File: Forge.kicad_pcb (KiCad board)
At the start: 2 copper layers, 2 parts, among them J1 USB_C_Receptacle_USB2.0_14P, U1 STM32F301C6Tx

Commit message: Began basic power design
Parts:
- added R1: 5k1, Resistor_SMD:R_0805_2012Metric_Pad1.20x1.40mm_HandSolder, F.Cu at (115.5, 99.0)
- added R2: 5k1, Resistor_SMD:R_0805_2012Metric_Pad1.20x1.40mm_HandSolder, F.Cu at (115.5, 101.9)
- added U2: AP2112K-3.3, Package_TO_SOT_SMD:SOT-23-5, F.Cu at (110.6, 99.9)
- added U3: USBLC6-2SC6, Package_TO_SOT_SMD:SOT-23-6, F.Cu at (110.6, 104.5)
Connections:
- net Net-(J1-GND-PadA1) renamed GND
- net Net-(J1-VBUS-PadA4) renamed +5V
- J1 pad A5: unconnected-(J1-CC1-PadA5) -> CC1
- J1 pad A6: unconnected-(J1-D+-PadA6) -> USB_Conn_D-
- J1 pad A7: unconnected-(J1-D--PadA7) -> USB_Conn_D+
- J1 pad B5: unconnected-(J1-CC2-PadB5) -> CC2
- J1 pad B6: unconnected-(J1-D+-PadB6) -> USB_Conn_D-
- J1 pad B7: unconnected-(J1-D--PadB7) -> USB_Conn_D+

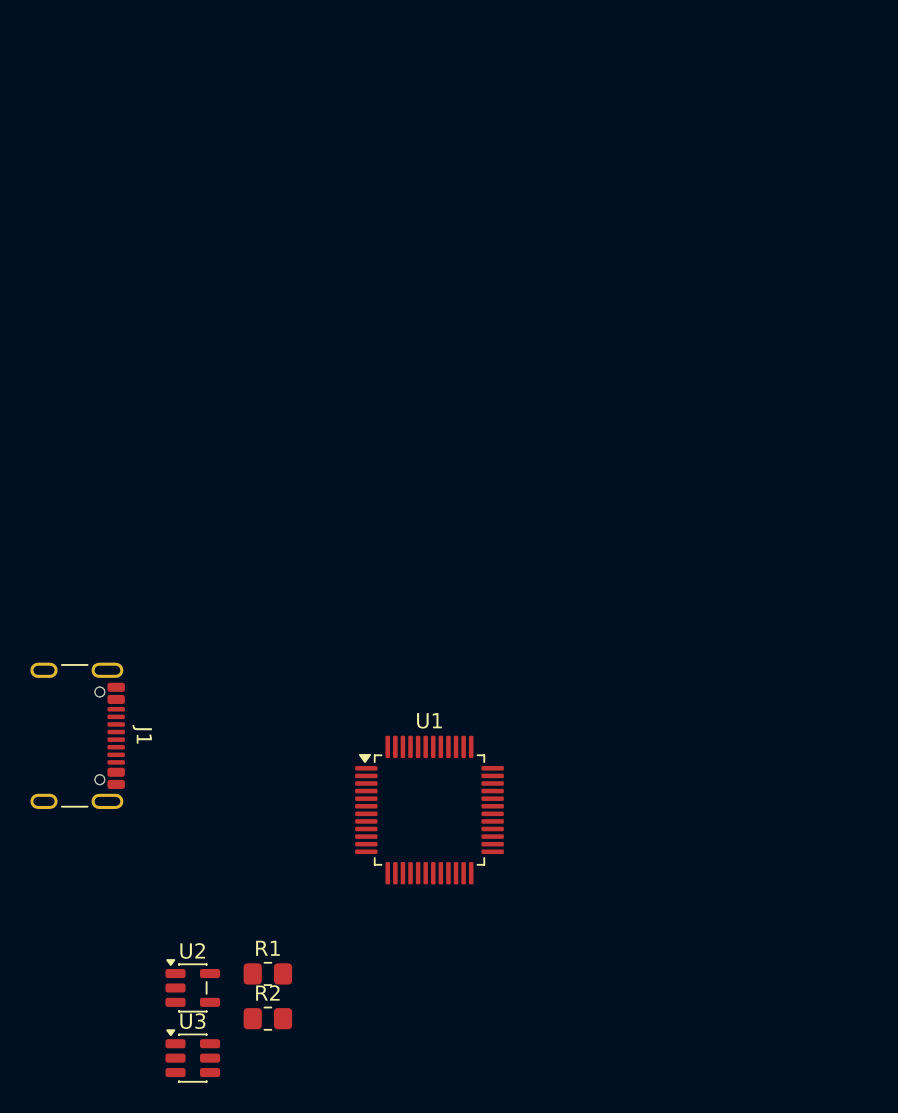
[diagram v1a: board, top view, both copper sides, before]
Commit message: Changed to MCU from stm32 to esp32 wroom for easier use for a first board
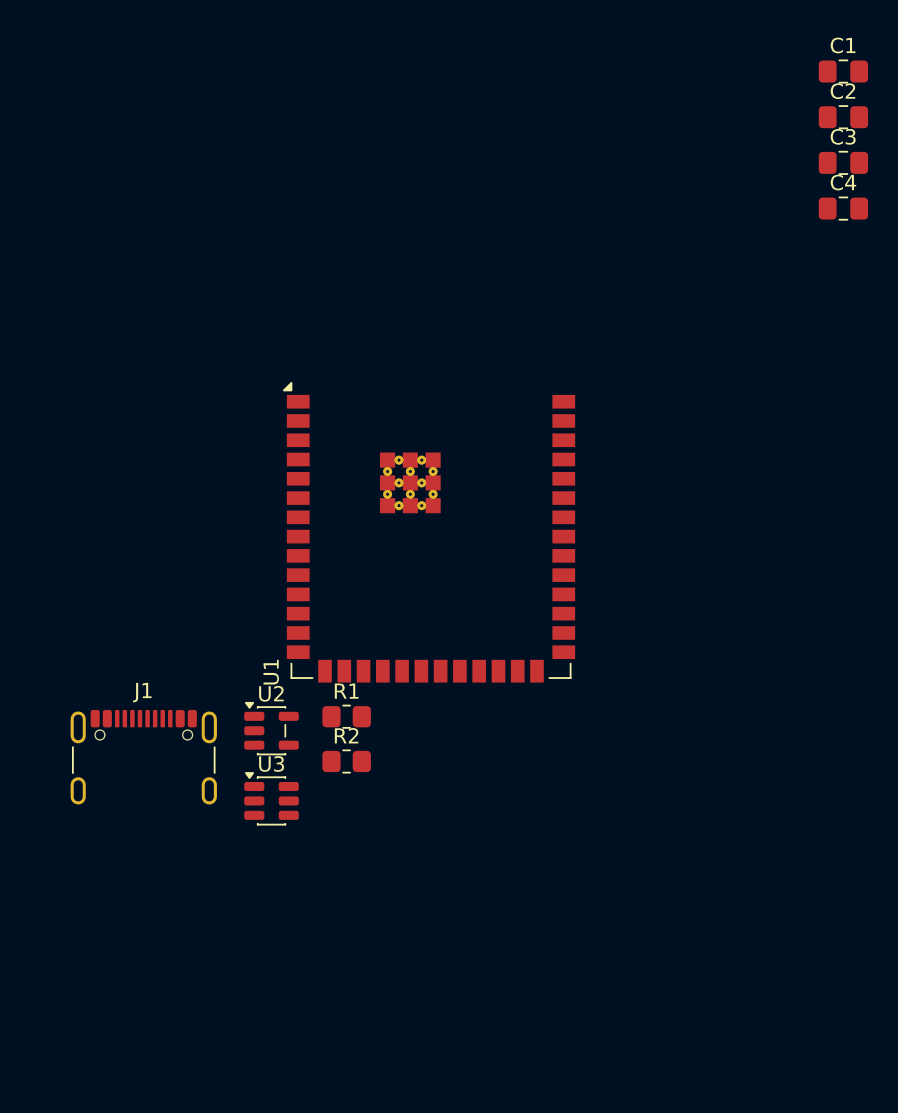
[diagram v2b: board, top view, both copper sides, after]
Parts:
- added C1: 1u, Capacitor_SMD:C_0805_2012Metric_Pad1.18x1.45mm_HandSolder, F.Cu at (153.5, 39.5)
- added C2: 1u, Capacitor_SMD:C_0805_2012Metric_Pad1.18x1.45mm_HandSolder, F.Cu at (153.5, 42.5)
- added C3: 100n, Capacitor_SMD:C_0805_2012Metric_Pad1.18x1.45mm_HandSolder, F.Cu at (153.5, 45.5)
- added C4: 10u, Capacitor_SMD:C_0805_2012Metric_Pad1.18x1.45mm_HandSolder, F.Cu at (153.5, 48.5)
- U1: value STM32F301C6Tx -> ESP32-S3-WROOM-2; footprint Package_QFP:LQFP-48_7x7mm_P0.5mm -> RF_Module:ESP32-S3-WROOM-2
- moved U1 21.7 mm to (126.3, 66.5)
- moved R2 17.7 mm to (120.7, 85.0)
- moved U2 17.7 mm to (115.8, 83.0)
- moved U3 17.7 mm to (115.8, 87.6)
- moved R1 17.7 mm to (120.7, 82.0)
- moved J1 6.06 mm to (107.3, 85.8), turned to 0 degrees
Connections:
- U1 pad 1: unconnected-(U1-VBAT-Pad1) -> GND
- U1 pad 12: unconnected-(U1-PA2-Pad12) -> I2C_SDA
- U1 pad 13: unconnected-(U1-PA3-Pad13) -> USB_D-
- U1 pad 14: unconnected-(U1-PA4-Pad14) -> USB_D+
- U1 pad 17: unconnected-(U1-PA7-Pad17) -> I2C_SCL
- U1 pad 18: unconnected-(U1-PB0-Pad18) -> SPI_CLK
- U1 pad 19: unconnected-(U1-PB1-Pad19) -> SPI_MOSI
- U1 pad 2: unconnected-(U1-PC13-Pad2) -> +3.3V
- U1 pad 20: unconnected-(U1-PB2-Pad20) -> SPI_MISO
- U1 pad 21: unconnected-(U1-PB10-Pad21) -> SPI_CS
- U1 pad 23: Net-(U1-VSS-Pad23) -> unconnected-(U1-IO21-Pad23)
- U1 pad 35: Net-(U1-VSS-Pad23) -> unconnected-(U1-MTMS/IO42-Pad35)
- U1 pad 40: unconnected-(U1-PB4-Pad40) -> GND
- U1 pad 41: unconnected-(U1-PB5-Pad41) -> GND
- U2 pad 1: unconnected-(U2-VIN-Pad1) -> +5V
- U2 pad 2: unconnected-(U2-GND-Pad2) -> GND
- U2 pad 3: unconnected-(U2-EN-Pad3) -> +5V
- U2 pad 5: unconnected-(U2-VOUT-Pad5) -> +3.3V

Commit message: Finished schematic ready for review
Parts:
- added C5: 100n, Capacitor_SMD:C_0805_2012Metric_Pad1.18x1.45mm_HandSolder, F.Cu at (161.5, 69.0)
- added C6: 100n, Capacitor_SMD:C_0805_2012Metric_Pad1.18x1.45mm_HandSolder, F.Cu at (144.0, 68.5)
- added C7: 10u, Capacitor_SMD:C_0805_2012Metric_Pad1.18x1.45mm_HandSolder, F.Cu at (146.5, 68.5)
- added C8: 100n, Capacitor_SMD:C_0603_1608Metric_Pad1.08x0.95mm_HandSolder, F.Cu at (161.0, 80.5)
- added C9: 100n, Capacitor_SMD:C_0603_1608Metric_Pad1.08x0.95mm_HandSolder, F.Cu at (165.0, 77.0)
- added J2: SWD, Connector_PinHeader_2.54mm:PinHeader_1x05_P2.54mm_Vertical, F.Cu at (133.5, 87.0)
- added J3: SPI, Connector_PinHeader_2.54mm:PinHeader_1x06_P2.54mm_Vertical, F.Cu at (161.7, 63.5)
- added J4: I2C, Connector_PinHeader_2.54mm:PinHeader_1x04_P2.54mm_Vertical, F.Cu at (148.9, 87.0)
- added Y1: Crystal_GND24, Crystal:Crystal_SMD_EuroQuartz_MT-4Pin_3.2x2.5mm_HandSoldering, F.Cu at (161.0, 77.0)
- C4: value 10u -> 100n
- U1: value ESP32-S3-WROOM-2 -> STM32F042K6Tx; footprint RF_Module:ESP32-S3-WROOM-2 -> Package_QFP:LQFP-32_7x7mm_P0.8mm
- moved C1 39.3 mm to (127.5, 69.0), turned to 90 degrees
- moved C4 32.6 mm to (156.5, 81.0), turned to -90 degrees
- moved C2 31.7 mm to (136.0, 69.0), turned to -90 degrees
- moved C3 27.2 mm to (161.5, 71.5)
- moved U1 26.5 mm to (151.5, 74.5), turned to 180 degrees
- moved U3 22.0 mm to (134.5, 76.0), turned to 90 degrees
- moved U2 21.6 mm to (131.9, 68.5)
- moved J1 16.7 mm to (120.0, 75.0), turned to -90 degrees
- moved R1 14.6 mm to (122.0, 67.5), turned to 180 degrees
- moved R2 2.49 mm to (121.0, 82.5), turned to 180 degrees
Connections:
- C3 pad 1: +3.3V -> NRST
- U1 pad 1: GND -> +3.3V
- U1 pad 10: unconnected-(U1-IO17-Pad10) -> SPI_NSS
- U1 pad 11: unconnected-(U1-IO18-Pad11) -> SPI_SCK
- U1 pad 12: I2C_SDA -> SPI_MISO
- U1 pad 13: USB_D- -> SPI_MOSI
- U1 pad 14: USB_D+ -> unconnected-(U1-PB0-Pad14)
- U1 pad 16: unconnected-(U1-IO46-Pad16) -> GND
- U1 pad 17: I2C_SCL -> +3.3V
- U1 pad 18: SPI_CLK -> unconnected-(U1-PA8-Pad18)
- U1 pad 19: SPI_MOSI -> unconnected-(U1-PA9-Pad19)
- U1 pad 2: +3.3V -> OSC_IN
- U1 pad 20: SPI_MISO -> unconnected-(U1-PA10-Pad20)
- U1 pad 21: SPI_CS -> USB_D-
- U1 pad 22: unconnected-(U1-IO14-Pad22) -> USB_D+
- U1 pad 23: unconnected-(U1-IO21-Pad23) -> SWDIO
- U1 pad 24: unconnected-(U1-IO47-Pad24) -> SWCLK
- U1 pad 29: unconnected-(U1-NC-Pad29) -> I2C_SCL
- U1 pad 3: unconnected-(U1-EN-Pad3) -> OSC_OUT
- U1 pad 30: unconnected-(U1-NC-Pad30) -> I2C_SDA
- U1 pad 31: unconnected-(U1-IO38-Pad31) -> BOOT0
- U1 pad 32: unconnected-(U1-MTCK/IO39-Pad32) -> GND
- U1 pad 4: unconnected-(U1-IO4-Pad4) -> NRST
- U1 pad 5: unconnected-(U1-IO5-Pad5) -> +3.3V
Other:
- board outline added: 51.5 x 32.5 mm

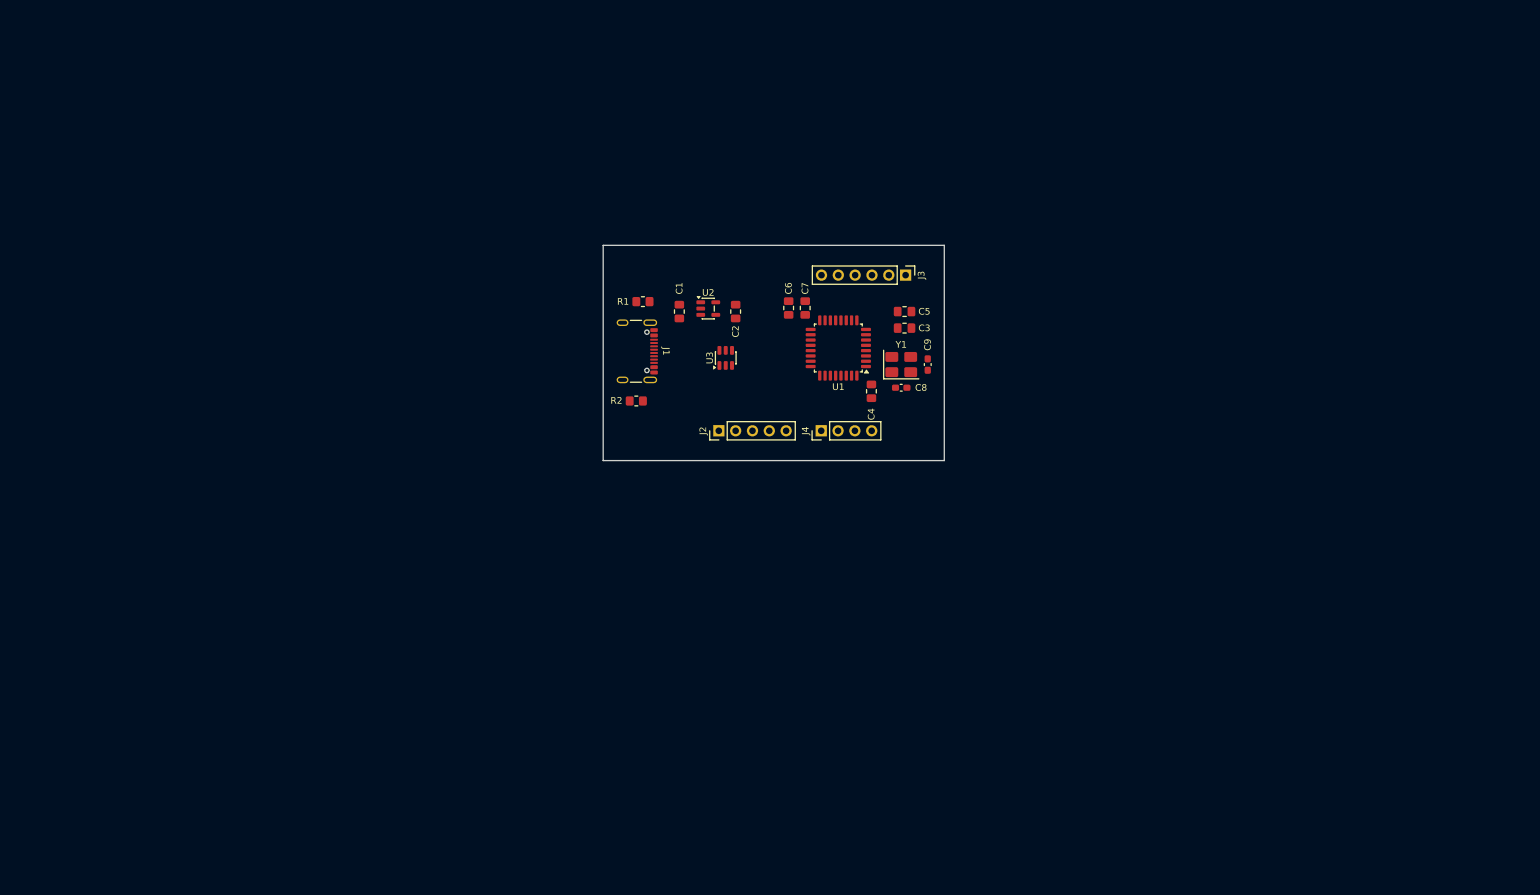
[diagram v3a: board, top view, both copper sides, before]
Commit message: Components placed based on the schematic layout
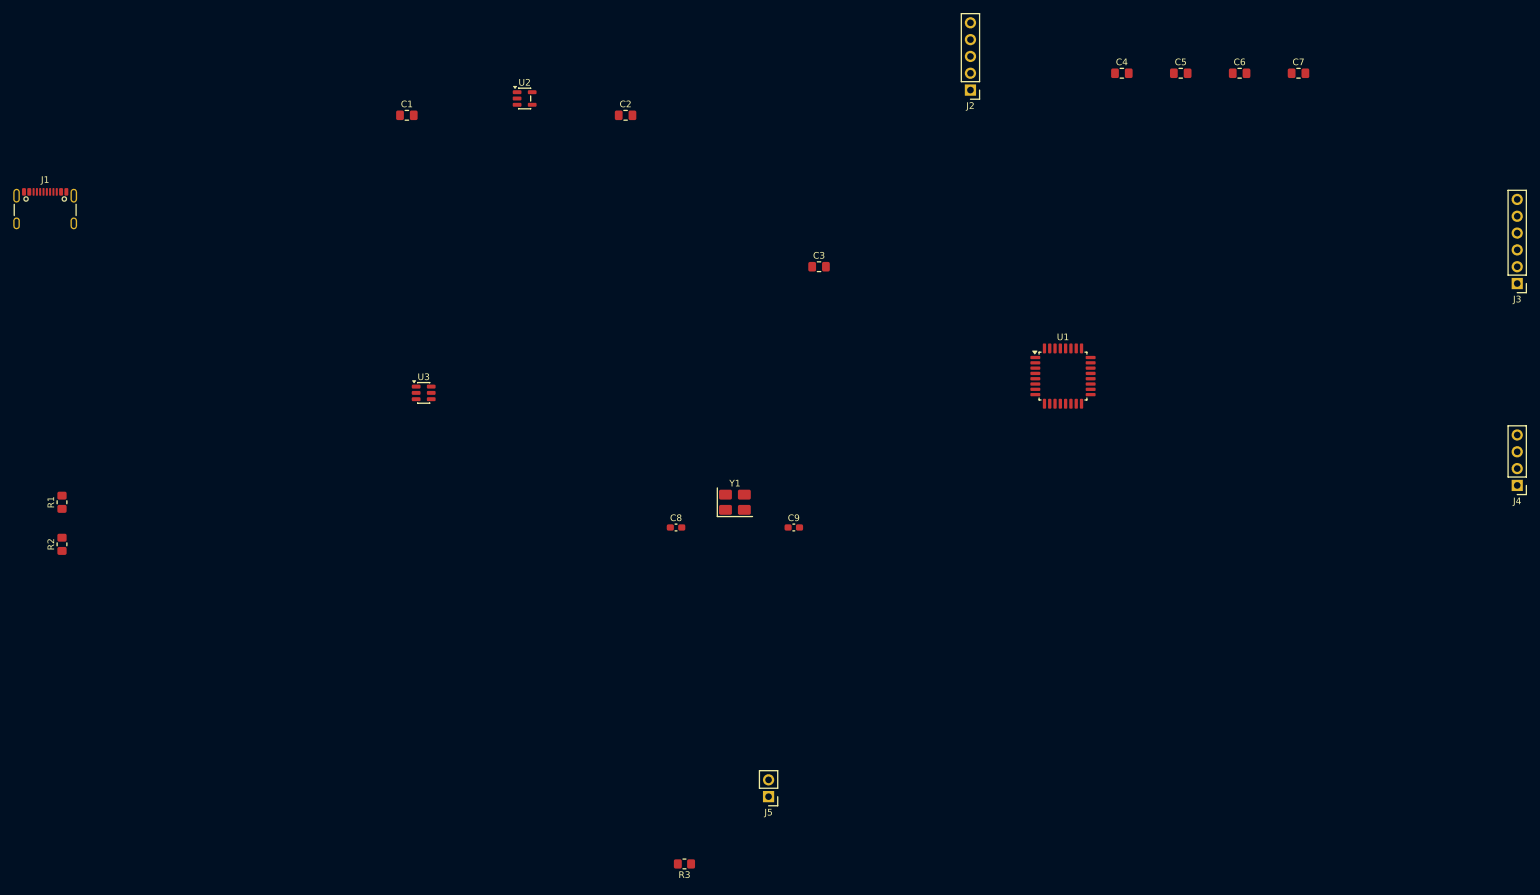
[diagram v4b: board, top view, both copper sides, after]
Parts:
- added J5: Boot0, Connector_PinHeader_2.54mm:PinHeader_1x02_P2.54mm_Vertical, F.Cu at (141.0, 142.2)
- added R3: 10k, Resistor_SMD:R_0805_2012Metric_Pad1.20x1.40mm_HandSolder, F.Cu at (128.3, 152.4)
- moved J4 105.4 mm to (254.0, 95.2), turned to 180 degrees
- moved R1 92.8 mm to (34.3, 97.8), turned to 90 degrees
- moved J3 92.3 mm to (254.0, 64.8), turned to 180 degrees
- moved J1 90.6 mm to (31.8, 54.6), turned to 0 degrees
- moved R2 89.4 mm to (34.3, 104.1), turned to 90 degrees
- moved C7 82.5 mm to (221.0, 33.0), turned to 0 degrees
- moved C6 76.8 mm to (212.1, 33.0), turned to 0 degrees
- moved J2 63.9 mm to (171.4, 35.6), turned to 180 degrees
- moved C4 61.1 mm to (194.3, 33.0), turned to 0 degrees
- moved C5 55.1 mm to (203.2, 33.0)
- moved C1 50.7 mm to (86.4, 39.4), turned to 0 degrees
- moved U3 45.9 mm to (88.9, 81.3), turned to 0 degrees
- moved U2 42.1 mm to (104.1, 36.8)
- moved C8 40.0 mm to (127.0, 101.6)
- moved U1 34.2 mm to (185.4, 78.7), turned to 0 degrees
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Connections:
- J2 pad 1: +3.3V -> GND
- J2 pad 2: SWDIO -> NRST
- J2 pad 4: NRST -> SWDIO
- J2 pad 5: GND -> +3.3V
- J3 pad 1: +3.3V -> GND
- J3 pad 2: SPI_NSS -> SPI_MOSI
- J3 pad 3: SPI_SCK -> SPI_MISO
- J3 pad 4: SPI_MISO -> SPI_SCK
- J3 pad 5: SPI_MOSI -> SPI_NSS
- J3 pad 6: GND -> +3.3V
- J4 pad 1: +3.3V -> GND
- J4 pad 2: I2C_SCL -> I2C_SDA
- J4 pad 3: I2C_SDA -> I2C_SCL
- J4 pad 4: GND -> +3.3V
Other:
- board outline removed
- board text added: "Main Sheet"
